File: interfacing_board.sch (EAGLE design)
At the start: 46 parts, among them IC1 MAX3096CSE, X1 87758-3816, X2 87758-3816

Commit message: Nucleo and ethernet module library components added. Implemented in schematics and PCB. Redesign of the PCB, errors removal.
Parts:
- removed ETHER: 332-10, con-garry:332-10
- removed X1, X2: 87758-3816, con-molex:87758-3816
- added U$1: ETHERNET, customy:ETHERNET
- added U$2: NUCLEOF103, customy:NUCLEOF103
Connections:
- removed net ADC12_IN8: X1-5.S
- removed net ADC12_IN9: X1-3.S
- removed net AGND: X2-7.S
- removed net AVDD: X2-32.S
- removed net BOOT0: X1-32.S
- removed net E5V: X1-33.S
- removed net INT: ETHER-2.S
- removed net IOREF: X1-27.S
- removed net NC: X1-13.S, X1-28.S, X1-29.S, X1-30.S, X2-1.S, X2-29.S, X2-3.S
- removed net PA1: X1-9.S
- removed net PA10: X2-6.S
- removed net PA11: X2-25.S
- removed net PA12: X2-27.S
- removed net PA13: X1-26.S
- removed net PA14: X1-24.S
- removed net PA15: X1-22.S
- removed net PA2: X2-4.S
- removed net PA3: X2-2.S
- removed net PA8: X2-16.S
- removed net PA9: X2-18.S
- removed net PB1: X2-15.S
- removed net PB10: X2-14.S
- removed net PB11: X2-21.S
- removed net PB12: X2-23.S
- removed net PB2: X2-17.S
- removed net PB3: X2-8.S
- removed net PB4: X2-12.S
- removed net PB5: X2-10.S
- removed net PB8: X2-36.S
- removed net PB9: X2-34.S
- removed net PC0: X1-1.S
- removed net PC13: X1-16.S
- removed net PC14: X1-14.S
- removed net PC15: X1-12.S
- removed net PC2: X1-4.S
- removed net PC3: X1-2.S
- removed net PC4: X2-5.S
- removed net PC5: X2-33.S
- removed net RESET: X1-25.S
- removed net SPI1_NSS: X1-7.S
- removed net U5V: X2-31.S
- removed net VBAT: X1-6.S
- removed net VDD: X1-34.S
- removed net VIN: X1-15.S
- new net ETH_INT: U$1.INT
- new net N$17: U$2.PC5
- new net N$20: U$2.PC4
- new net N$21: U$2.PC3
- new net N$22: U$2.PC2
- new net N$23: U$2.PC1
- new net N$24: U$2.PC0
- new net N$28: U$2.RESET
- new net N$29: U$2.BOOT0
- new net N$3: U$2.PC15
- new net N$30: U$2.IOREF
- new net N$34: U$2.PA1
- new net N$35: U$2.PA2
- new net N$36: U$2.PA3
- new net N$37: U$2.PA4
- new net N$4: U$1.WOL
- new net N$41: U$2.PA8
- new net N$42: U$2.PA9
- new net N$43: U$2.PA10
- new net N$44: U$2.PA11
- new net N$45: U$2.PA12
- new net N$46: U$2.PA13
- new net N$47: U$2.PA14
- new net N$48: U$2.PA15
- new net N$49: U$2.PB0
- new net N$5: U$2.PC14
- new net N$50: U$2.PB1
- new net N$51: U$2.PB2
- new net N$52: U$2.PB3
- new net N$53: U$2.PB4
- new net N$54: U$2.PB5
- new net N$59: U$2.PB10
- new net N$60: U$2.PB11
- new net N$61: U$2.PB12
- net +5V: no longer X1-21.S
- net 3.3V: now also U$1.VCC, U$2.3V3; no longer ALBEDO1-1.S, ALBEDO2-1.S, ETHER-9.S, UV1-1.S, VIS1-1.S, X1-23.S
- net 5V: now also ALBEDO1-1.S, ALBEDO2-1.S, UV1-1.S, VIS1-1.S
- net CHA-1L: now also U$2.PB8
- net CHB-1L: now also U$2.PB9
- net CHC-1L: now also U$2.PA0; no longer X1-11.S
- net CLKOUT: now also U$1.CLKOUT; no longer ETHER-1.S
- net CS_ETH: now also U$1.CS, U$2.PC11; no longer ETHER-7.S, X1-37.S
- net CS_HTP: now also U$2.PC13
- net CS_HTP2: now also U$2.PC8; no longer X2-37.S
- net CS_IMU: now also U$2.PC12; no longer X1-36.S
- net CS_RTC: now also U$2.PC9; no longer X2-38.S
- net CS_SD: now also U$2.PC10; no longer X1-38.S
- net ETH_RES: now also U$1.RESET, U$2.PD0; no longer ETHER-8.S, X1-10.S
- net GND: now also U$1.GND, U$2.GND, U$2.GND2, U$2.GND3, U$2.GND4, U$2.GND5, U$2.GND6; no longer ETHER-10.S, X1-17.S, X1-19.S, X1-20.S, X1-31.S, X2-19.S, X2-30.S
- net IND1: now also U$2.PC6; no longer X2-35.S
- net IND2: now also U$2.PC7; no longer X2-20.S
- net M11: now also U$2.PD1; no longer X1-8.S
- net M12: now also U$2.PD2; no longer X1-35.S
- net SCL1: now also U$2.PB6; no longer X2-22.S
- net SDA1: now also U$2.PB7; no longer X1-18.S
- net SPI1_MISO: now also U$1.SO, U$2.PA6; no longer ETHER-4.S, X2-26.S
- net SPI1_MOSI: now also U$1.SI, U$2.PA7; no longer ETHER-5.S, X2-24.S
- net SPI1_SCK: now also U$1.SCK, U$2.PA5; no longer ETHER-6.S, X2-28.S
- net SPI2_MISO: now also U$2.PB14; no longer X2-11.S
- net SPI2_MOSI: now also U$2.PB15; no longer X2-13.S
- net SPI2_SCK: now also U$2.PB13; no longer X2-9.S
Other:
- note removed: "H-bridges: VM pin"
- note removed: "to do:"
- moved on the sheet: ENDR1-1, ENDR1-10, ENDR1-2, ENDR1-3, ENDR1-4, ENDR1-5, ENDR1-6, ENDR1-7, ENDR1-8, ENDR1-9, R10, R11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

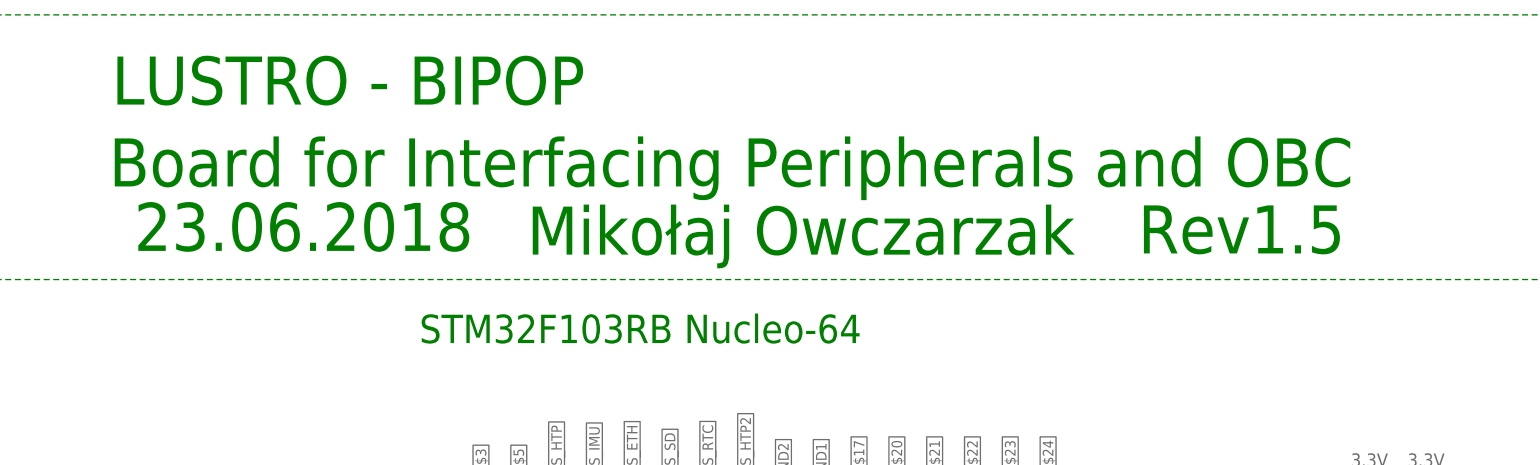
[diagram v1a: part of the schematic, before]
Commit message: SGlux version of transducer, new lib elements, transVIS deleted
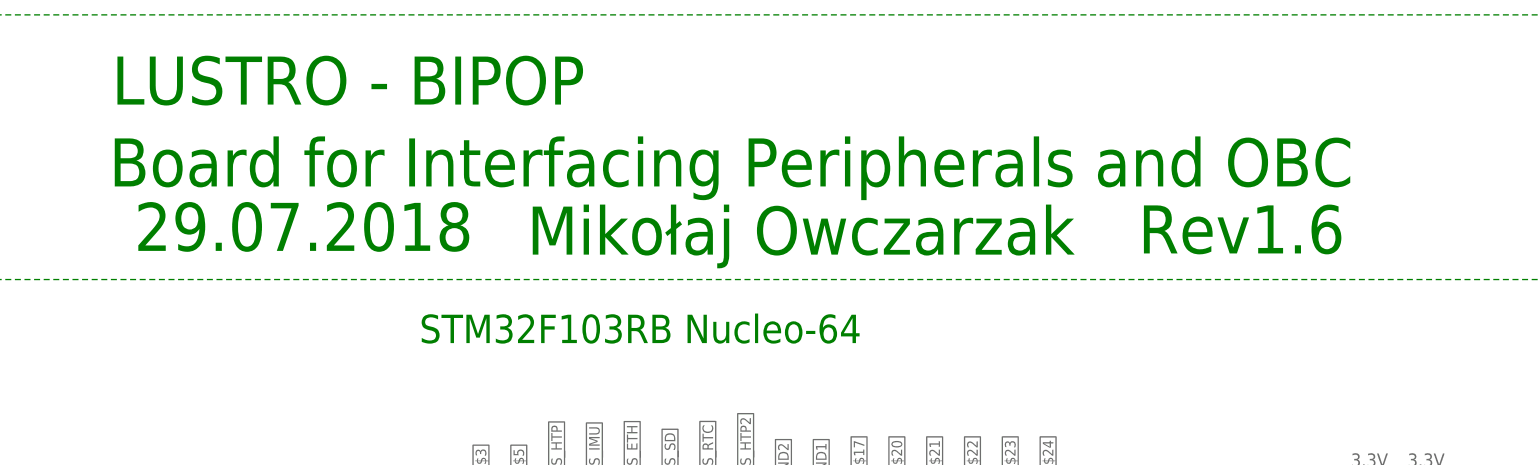
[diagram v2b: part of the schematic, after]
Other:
- note added: "29.07.2018"
- note added: "Rev1.6"
- note removed: "23.06.2018"
- note removed: "Rev1.5"
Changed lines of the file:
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@@
 <text x="24.327021875" y="-48.43301875" size="3.81" layer="91">Motor's driver</text>
 <text x="-100.78511875" y="263.968075" size="6.4516" layer="91">Board for Interfacing Peripherals and OBC</text>
-<text x="37.49488125" y="254.968075" size="6.4516" layer="91">Rev1.5</text>
+<text x="37.49488125" y="254.968075" size="6.4516" layer="91">Rev1.6</text>
 <text x="-100.42511875" y="274.968075" size="6.4516" layer="91">LUSTRO - BIPOP</text>
-<text x="-97.42511875" y="255.308075" size="6.4516" layer="91">23.06.2018</text>
+<text x="-97.42511875" y="255.308075" size="6.4516" layer="91">29.07.2018</text>
 <text x="-44.62511875" y="254.808075" size="6.4516" layer="91">Mikołaj Owczarzak</text>
 <text x="-89.112978125" y="-49.69301875" size="3.81" layer="91">Rotation indicators' sockets</text>

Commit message: Further footprint updates, BIPOP v. 1.8 ready to order.
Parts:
- removed ENDR1: 332-10, con-garry:332-10
- removed OPTO6: 332-04, con-garry:332-04
- added OPTO2: (no value), pinhead:PINHD-2X2
- added R24, R8: (no value), resistor:R-EU_M0805
- added U$3: ENX10, customy:ENX10
- ALBEDO1, ALBEDO2, UV1, VIS1: value 22-05-7048-04 -> 22-27-2041-04; device EP_molex_6410_7395:22-05-7048-04 -> EP_molex_6410_7395:22-27-2041-04
- OPTO1: value 332-04 -> (none); device con-garry:332-04 -> pinhead:PINHD-2X2
- SD: value 22-23-2071 -> SD_2597; device con-molex:22-23-2071 -> customy:SD_2597
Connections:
- net N$18 renamed REC_PULLUP
- net N$19 renamed REC_PULLDOWN
- removed net +5V: R1.1
- new net ~INCHC1: U$3.!CHC
- net 3.3V: now also ALBEDO1-1.S, ALBEDO2-1.S, R24.2, R8.2, SD.VDD2, UV1-1.S, VIS1-1.S; no longer SD-6.S
- net 5V: now also R1.1, U$3.VCC; no longer ALBEDO1-1.S, ALBEDO2-1.S, ENDR1-2.S, UV1-1.S, VIS1-1.S
- net CD_SD: now also SD.DETECT; no longer SD-1.S
- net CS_ETH: now also R24.1
- net CS_SD: now also R8.1, SD.CS; no longer SD-2.S
- net GND: now also OPTO1.3, OPTO2.3, SD.GND2, U$3.GND; no longer ENDR1-3.S, OPTO1-2.S, OPTO6-2.S, SD-7.S
- net INCHA-1: now also U$3.CHA; no longer ENDR1-6.S
- net INCHB-1: now also U$3.CHB; no longer ENDR1-8.S
- net INCHC-1: now also U$3.CHC; no longer ENDR1-10.S
- net IND1: now also OPTO1.4; no longer OPTO1-1.S
- net IND2: now also OPTO2.4; no longer OPTO6-1.S
- net N$12: now also OPTO2.2; no longer OPTO6-3.S
- net N$15: now also OPTO2.1; no longer OPTO6-4.S
- net N$2: now also OPTO1.2; no longer OPTO1-3.S
- net N$7: now also OPTO1.1; no longer OPTO1-4.S
- net SPI1_MISO: now also SD.DO; no longer SD-4.S
- net SPI1_MOSI: now also SD.DI; no longer SD-5.S
- net SPI1_SCK: now also SD.SCLK; no longer SD-3.S
- net ~INCHA-1: now also U$3.!CHA; no longer ENDR1-5.S
- net ~INCHB-1: now also U$3.!CHB; no longer ENDR1-7.S
- net ~INCHC-1: no longer ENDR1-9.S
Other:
- note added: "15.08.2018"
- note added: "Rev1.7"
- note removed: "29.07.2018"
- note removed: "Rev1.6"
- moved on the sheet: ALBEDO1-1, ALBEDO1-2, ALBEDO1-3, ALBEDO1-4, ALBEDO2-2, ALBEDO2-3, ALBEDO2-4, UV1-2, UV1-3, UV1-4, VIS1-2, VIS1-3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

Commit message: poprawione routowanie
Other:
- moved on the sheet: IMU-1, IMU-2, IMU-3, IMU-4, IMU-5, IMU-6, IMU-7, IMU-8, R10, R11, R12, R13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

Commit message: refit
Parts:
- removed ALBEDO1, ALBEDO2, UV1, VIS1: 22-27-2041-04, EP_molex_6410_7395:22-27-2041-04
- removed DRV_: DRV8871, customy:DRV8871
- removed HTP1, HTP2: 22-27-2071-07, EP_molex_6410_7395:22-27-2071-07
- removed IMU: 22-27-2081-08, EP_molex_6410_7395:22-27-2081-08
- removed OPTO1, OPTO2: (no value), pinhead:PINHD-2X2
- removed POWER: MSTBA6, con-phoenix-508:MSTBA6
- removed RTC_: RTC_WAVESHARE, SKA_EP_molex_6410_7395:RTC_WAVESHARE
- removed SD: SD_2597, customy:SD_2597
- removed U$1: ETHERNET, customy:ETHERNET
- removed U$2: NUCLEOF103, customy:NUCLEOF103
- removed U$3: ENX10, customy:ENX10
- added JP10, JP11: 22-27-2071-07, EP_molex_6410_7395:22-27-2071-07
- added JP12: SD_2597, customy:SD_2597
- added JP13, JP14: (no value), pinhead:PINHD-2X2
- added JP15: ENX10, customy:ENX10
- added JP16: RTC_WAVESHARE, customy:RTC_WAVESHARE
- added JP1A: JP1B, customy:NUCLEOF103
- added JP2: ETHERNET, customy:ETHERNET
- added JP3: 22-27-2081-08, EP_molex_6410_7395:22-27-2081-08
- added JP4: DRV8871, customy:DRV8871
- added JP5, JP6, JP7, JP8: 22-27-2041-04, EP_molex_6410_7395:22-27-2041-04
- added JP9: MSTBA6, con-phoenix-508:MSTBA6
- R10, R11, R18, R28, R33, R9: value 4.7k -> 2k49
- R12, R13, R14, R15, R19, R27: value 5k -> 2k49
- R16, R20, R22: value 10k -> 20k
- R17, R21, R7: value 5k -> 10k
- R23, R64: value (none) -> 47k
- R24, R8: value (none) -> 2k49
- R5, R62: value (none) -> 82k
- R6, R63: value (none) -> 5k
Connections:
- removed net N$17: U$2.PC5
- removed net N$20: U$2.PC4
- removed net N$21: U$2.PC3
- removed net N$22: U$2.PC2
- removed net N$23: U$2.PC1
- removed net N$24: U$2.PC0
- removed net N$3: U$2.PC15
- removed net N$34: U$2.PA1
- removed net N$35: U$2.PA2
- removed net N$36: U$2.PA3
- removed net N$37: U$2.PA4
- removed net N$41: U$2.PA8
- removed net N$42: U$2.PA9
- removed net N$43: U$2.PA10
- removed net N$44: U$2.PA11
- removed net N$45: U$2.PA12
- removed net N$46: U$2.PA13
- removed net N$47: U$2.PA14
- removed net N$48: U$2.PA15
- removed net N$49: U$2.PB0
- removed net N$5: U$2.PC14
- removed net N$50: U$2.PB1
- removed net N$51: U$2.PB2
- removed net N$52: U$2.PB3
- removed net N$53: U$2.PB4
- removed net N$54: U$2.PB5
- removed net N$59: U$2.PB10
- removed net N$60: U$2.PB11
- removed net N$61: U$2.PB12
- net 12V: now also JP4.M-VCC, JP9-5.1; no longer DRV_MOT_VCC.S, POWER-5.1
- net 3.3V: now also JP10-7.S, JP11-7.S, JP12.VDD2, JP16.VCC, JP1A.3V3, JP2.VCC, JP3-7.S, JP5-1.S, JP6-1.S, JP7-1.S, JP8-1.S, JP9-1.1; no longer ALBEDO1-1.S, ALBEDO2-1.S, HTP1-7.S, HTP2-7.S, IMU-7.S, POWER-1.1, RTC_RTCVCC.1, SD.VDD2, U$1.VCC, U$2.3V3, UV1-1.S, VIS1-1.S
- net 3V_O: now also JP10-6.S; no longer HTP1-6.S
- net 3V_O2: now also JP11-6.S; no longer HTP2-6.S
- net 5V: now also JP15.VCC, JP9-3.1; no longer POWER-3.1, U$3.VCC
- net CD_SD: now also JP12.DETECT; no longer SD.DETECT
- net CHA-1L: now also JP1A.PB8; no longer U$2.PB8
- net CHB-1L: now also JP1A.PB9; no longer U$2.PB9
- net CHC-1L: now also JP1A.PA0; no longer U$2.PA0
- net CLKOUT: now also JP2.CLKOUT; no longer U$1.CLKOUT
- net CS_ETH: now also JP1A.PC11, JP2.CS; no longer U$1.CS, U$2.PC11
- net CS_HTP: now also JP10-1.S, JP1A.PC13; no longer HTP1-1.S, U$2.PC13
- net CS_HTP2: now also JP11-1.S, JP1A.PC8; no longer HTP2-1.S, U$2.PC8
- net CS_IMU: now also JP1A.PC12, JP3-1.S; no longer IMU-1.S, U$2.PC12
- net CS_RTC: now also JP16.CS, JP1A.PC9; no longer RTC_RTCCS.1, U$2.PC9
- net CS_SD: now also JP12.CS, JP1A.PC10; no longer SD.CS, U$2.PC10
- net DRV1-VM: now also JP4.VM; no longer DRV_VM.1
- net ETH_INT: now also JP2.INT; no longer U$1.INT
- net ETH_RES: now also JP1A.PD0, JP2.RESET; no longer U$1.RESET, U$2.PD0
- net GND: now also JP10-5.S, JP11-5.S, JP12.GND2, JP13.3, JP14.3, JP15.GND, JP16.GND, JP1A.GND, JP1A.GND2, JP1A.GND3, JP1A.GND4, JP1A.GND5, JP1A.GND6, JP2.GND, JP3-5.S, JP3-8.S, JP4.GND, JP4.M-GND, JP5-4.S, JP6-4.S, JP7-4.S, JP8-4.S, JP9-2.1, JP9-4.1, JP9-6.1; no longer ALBEDO1-4.S, ALBEDO2-4.S, DRV_GND.1, DRV_MOT_GND.S, HTP1-5.S, HTP2-5.S, IMU-5.S, IMU-8.S, OPTO1.3, OPTO2.3, POWER-2.1, POWER-4.1, POWER-6.1, RTC_RTCGND.1, SD.GND2, U$1.GND, U$2.GND, U$2.GND2, U$2.GND3, U$2.GND4, U$2.GND5, U$2.GND6, U$3.GND, UV1-4.S, VIS1-4.S
- net IMU_INT: now also JP3-6.S; no longer IMU-6.S
- net INCHA-1: now also JP15.CHA; no longer U$3.CHA
- net INCHB-1: now also JP15.CHB; no longer U$3.CHB
- net INCHC-1: now also JP15.CHC; no longer U$3.CHC
- net IND1: now also JP13.4, JP1A.PC6; no longer OPTO1.4, U$2.PC6
- net IND2: now also JP14.4, JP1A.PC7; no longer OPTO2.4, U$2.PC7
- net M11: now also JP1A.PD1, JP4.IN1; no longer DRV_IN1.1, U$2.PD1
- net M12: now also JP1A.PD2, JP4.IN2; no longer DRV_IN2.1, U$2.PD2
- net N$12: now also JP14.2; no longer OPTO2.2
- net N$15: now also JP14.1; no longer OPTO2.1
- net N$2: now also JP13.2; no longer OPTO1.2
- net N$28: now also JP1A.RESET; no longer U$2.RESET
- net N$29: now also JP1A.BOOT0; no longer U$2.BOOT0
- net N$30: now also JP1A.IOREF; no longer U$2.IOREF
- net N$4: now also JP2.WOL; no longer U$1.WOL
- net N$7: now also JP13.1; no longer OPTO1.1
- net SCL1: now also JP1A.PB6, JP5-3.S, JP6-3.S, JP7-3.S, JP8-3.S; no longer ALBEDO1-3.S, ALBEDO2-3.S, U$2.PB6, UV1-3.S, VIS1-3.S
- net SDA1: now also JP1A.PB7, JP5-2.S, JP6-2.S, JP7-2.S, JP8-2.S; no longer ALBEDO1-2.S, ALBEDO2-2.S, U$2.PB7, UV1-2.S, VIS1-2.S
- net SPI1_MISO: now also JP12.DO, JP1A.PA6, JP2.SO; no longer SD.DO, U$1.SO, U$2.PA6
- net SPI1_MOSI: now also JP12.DI, JP1A.PA7, JP2.SI; no longer SD.DI, U$1.SI, U$2.PA7
- net SPI1_SCK: now also JP12.SCLK, JP1A.PA5, JP2.SCK; no longer SD.SCLK, U$1.SCK, U$2.PA5
- net SPI2_MISO: now also JP10-3.S, JP11-3.S, JP16.MISO, JP1A.PB14, JP3-4.S; no longer HTP1-3.S, HTP2-3.S, IMU-4.S, RTC_RTCMISO.1, U$2.PB14
- net SPI2_MOSI: now also JP10-2.S, JP11-2.S, JP16.MOSI, JP1A.PB15, JP3-3.S; no longer HTP1-2.S, HTP2-2.S, IMU-3.S, RTC_RTCMOSI.1, U$2.PB15
- net SPI2_SCK: now also JP10-4.S, JP11-4.S, JP16.SCK, JP1A.PB13, JP3-2.S; no longer HTP1-4.S, HTP2-4.S, IMU-2.S, RTC_RTCSCK.1, U$2.PB13
- net ~INCHA-1: now also JP15.!CHA; no longer U$3.!CHA
- net ~INCHB-1: now also JP15.!CHB; no longer U$3.!CHB
- net ~INCHC1: now also JP15.!CHC; no longer U$3.!CHC
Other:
- moved on the sheet: IC1, R1, R10, R11, R12, R13, R14, R15, R16, R17, R18, R19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
